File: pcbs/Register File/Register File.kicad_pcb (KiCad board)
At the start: 4 copper layers, 208 parts, among them U201 74HCT574, U202 74HC245, U203 74HC245, U204 74HC245, U301 74HCT574, U302 74HC245, U303 74HC245, U304 74HC245, U401 74HCT574, U402 74HC245, U403 74HC245, U404 74HC245, U501 74HCT574, U502 74HC245, U503 74HC245, U504 74HC245, U601 74HCT574, U602 74HC245, U603 74HC245, U604 74HC245, U701 74HCT574, U702 74HC245, U703 74HC245, U704 74HC245, U801 74HCT574, U802 74HC245, U803 74HC245, U804 74HC245, U901 74HCT574, U902 74HC245, U903 74HC245, U904 74HC245

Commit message: More work
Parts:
- moved U902 87.7 mm to (248.9, 61.0)
- moved R408 71.6 mm to (119.4, 45.7)
- moved R407 71.6 mm to (119.4, 43.2)
- moved R406 71.6 mm to (119.4, 40.6)
- moved R405 71.5 mm to (119.4, 38.1)
- moved R404 71.5 mm to (119.4, 35.6)
- moved R403 71.5 mm to (119.4, 33.0)
- moved R402 71.4 mm to (119.4, 30.5)
- moved R401 71.4 mm to (119.4, 27.9)
- moved D402 71.2 mm to (114.3, 30.5)
- moved D401 71.2 mm to (114.3, 27.9)
- moved D403 71.1 mm to (114.3, 33.0)
- moved D404 71.0 mm to (114.3, 35.6)
- moved D405 71.0 mm to (114.3, 38.1)
- moved D406 70.9 mm to (114.3, 40.6)
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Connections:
- U201 pad 10: unconnected-(U201-GND-Pad10) -> GND
- U201 pad 20: unconnected-(U201-VCC-Pad20) -> +5V
- U202 pad 10: unconnected-(U202-GND-Pad10) -> GND
- U202 pad 20: unconnected-(U202-VCC-Pad20) -> +5V
- U203 pad 10: unconnected-(U203-GND-Pad10) -> GND
- U203 pad 20: unconnected-(U203-VCC-Pad20) -> +5V
- U204 pad 10: unconnected-(U204-GND-Pad10) -> GND
- U204 pad 20: unconnected-(U204-VCC-Pad20) -> +5V
- U301 pad 10: unconnected-(U301-GND-Pad10) -> GND
- U301 pad 20: unconnected-(U301-VCC-Pad20) -> +5V
- U302 pad 10: unconnected-(U302-GND-Pad10) -> GND
- U302 pad 20: unconnected-(U302-VCC-Pad20) -> +5V
- U303 pad 10: unconnected-(U303-GND-Pad10) -> GND
- U303 pad 20: unconnected-(U303-VCC-Pad20) -> +5V
- U304 pad 10: unconnected-(U304-GND-Pad10) -> GND
- U304 pad 20: unconnected-(U304-VCC-Pad20) -> +5V
- U401 pad 10: unconnected-(U401-GND-Pad10) -> GND
- U401 pad 20: unconnected-(U401-VCC-Pad20) -> +5V
- U402 pad 10: unconnected-(U402-GND-Pad10) -> GND
- U402 pad 20: unconnected-(U402-VCC-Pad20) -> +5V
- U403 pad 10: unconnected-(U403-GND-Pad10) -> GND
- U403 pad 20: unconnected-(U403-VCC-Pad20) -> +5V
- U404 pad 10: unconnected-(U404-GND-Pad10) -> GND
- U404 pad 20: unconnected-(U404-VCC-Pad20) -> +5V
- U501 pad 10: unconnected-(U501-GND-Pad10) -> GND
- U501 pad 20: unconnected-(U501-VCC-Pad20) -> +5V
- U502 pad 10: unconnected-(U502-GND-Pad10) -> GND
- U502 pad 20: unconnected-(U502-VCC-Pad20) -> +5V
- U503 pad 10: unconnected-(U503-GND-Pad10) -> GND
- U503 pad 20: unconnected-(U503-VCC-Pad20) -> +5V
- U504 pad 10: unconnected-(U504-GND-Pad10) -> GND
- U504 pad 20: unconnected-(U504-VCC-Pad20) -> +5V
- U601 pad 10: unconnected-(U601-GND-Pad10) -> GND
- U601 pad 2: /Register 4/C0 -> /Register 0/C0
- U601 pad 20: unconnected-(U601-VCC-Pad20) -> +5V
- U601 pad 3: /Register 4/C1 -> /Register 0/C1
- U601 pad 4: /Register 4/C2 -> /Register 0/C2
- U601 pad 5: /Register 4/C3 -> /Register 0/C3
- U601 pad 6: /Register 4/C4 -> /Register 0/C4
- U601 pad 7: /Register 4/C5 -> /Register 0/C5
- U601 pad 8: /Register 4/C6 -> /Register 0/C6
- U601 pad 9: /Register 4/C7 -> /Register 0/C7
- U602 pad 10: unconnected-(U602-GND-Pad10) -> GND
- U602 pad 11: /Register 4/A7 -> /Register 0/A7
- U602 pad 12: /Register 4/A6 -> /Register 0/A6
- U602 pad 13: /Register 4/A5 -> /Register 0/A5
- U602 pad 14: /Register 4/A4 -> /Register 0/A4
- U602 pad 15: /Register 4/A3 -> /Register 0/A3
- U602 pad 16: /Register 4/A2 -> /Register 0/A2
- U602 pad 17: /Register 4/A1 -> /Register 0/A1
- U602 pad 18: /Register 4/A0 -> /Register 0/A0
- U602 pad 20: unconnected-(U602-VCC-Pad20) -> +5V
- U603 pad 10: unconnected-(U603-GND-Pad10) -> GND
- U603 pad 11: /Register 4/B7 -> /Register 0/B7
- U603 pad 12: /Register 4/B6 -> /Register 0/B6
- U603 pad 13: /Register 4/B5 -> /Register 0/B5
- U603 pad 14: /Register 4/B4 -> /Register 0/B4
- U603 pad 15: /Register 4/B3 -> /Register 0/B3
- U603 pad 16: /Register 4/B2 -> /Register 0/B2
- U603 pad 17: /Register 4/B1 -> /Register 0/B1
- U603 pad 18: /Register 4/B0 -> /Register 0/B0
- U603 pad 20: unconnected-(U603-VCC-Pad20) -> +5V
- U604 pad 10: unconnected-(U604-GND-Pad10) -> GND
- U604 pad 11: /Register 4/C7 -> /Register 0/C7
- U604 pad 12: /Register 4/C6 -> /Register 0/C6
- U604 pad 13: /Register 4/C5 -> /Register 0/C5
- U604 pad 14: /Register 4/C4 -> /Register 0/C4
- U604 pad 15: /Register 4/C3 -> /Register 0/C3
- U604 pad 16: /Register 4/C2 -> /Register 0/C2
- U604 pad 17: /Register 4/C1 -> /Register 0/C1
- U604 pad 18: /Register 4/C0 -> /Register 0/C0
- U604 pad 20: unconnected-(U604-VCC-Pad20) -> +5V
- U701 pad 10: unconnected-(U701-GND-Pad10) -> GND
- U701 pad 20: unconnected-(U701-VCC-Pad20) -> +5V
- U702 pad 10: unconnected-(U702-GND-Pad10) -> GND
- U702 pad 20: unconnected-(U702-VCC-Pad20) -> +5V
- U703 pad 10: unconnected-(U703-GND-Pad10) -> GND
- U703 pad 20: unconnected-(U703-VCC-Pad20) -> +5V
- U704 pad 10: unconnected-(U704-GND-Pad10) -> GND
- U704 pad 20: unconnected-(U704-VCC-Pad20) -> +5V
- U801 pad 10: unconnected-(U801-GND-Pad10) -> GND
- U801 pad 20: unconnected-(U801-VCC-Pad20) -> +5V
- U802 pad 10: unconnected-(U802-GND-Pad10) -> GND
- U802 pad 20: unconnected-(U802-VCC-Pad20) -> +5V
- U803 pad 10: unconnected-(U803-GND-Pad10) -> GND
- U803 pad 20: unconnected-(U803-VCC-Pad20) -> +5V
- U804 pad 10: unconnected-(U804-GND-Pad10) -> GND
- U804 pad 20: unconnected-(U804-VCC-Pad20) -> +5V
- U901 pad 10: unconnected-(U901-GND-Pad10) -> GND
- U901 pad 20: unconnected-(U901-VCC-Pad20) -> +5V
- U902 pad 10: unconnected-(U902-GND-Pad10) -> GND
- U902 pad 20: unconnected-(U902-VCC-Pad20) -> +5V
- U903 pad 10: unconnected-(U903-GND-Pad10) -> GND
- U903 pad 20: unconnected-(U903-VCC-Pad20) -> +5V
- U904 pad 10: unconnected-(U904-GND-Pad10) -> GND
- U904 pad 20: unconnected-(U904-VCC-Pad20) -> +5V
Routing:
- net /Register 4/r0: track 0.00 -> 107.5 mm, vias 0 -> 3
- net /Register 5/r0: track 0.00 -> 107.5 mm, vias 0 -> 3
- net /Register 7/r0: track 0.00 -> 107.5 mm, vias 0 -> 3
- net /Register 6/r0: track 0.00 -> 107.5 mm, vias 0 -> 3
- net /Register 5/r1: track 0.00 -> 103.2 mm, vias 0 -> 3
- net /Register 6/r1: track 0.00 -> 103.2 mm, vias 0 -> 3
- net /Register 4/r1: track 0.00 -> 103.2 mm, vias 0 -> 3
- net /Register 7/r1: track 0.00 -> 103.2 mm, vias 0 -> 3
- net /Register 5/r2: track 0.00 -> 98.8 mm, vias 0 -> 3
- net /Register 4/r2: track 0.00 -> 98.8 mm, vias 0 -> 3
- net /Register 7/r2: track 0.00 -> 98.8 mm, vias 0 -> 3
- net /Register 6/r2: track 0.00 -> 98.8 mm, vias 0 -> 3
- net /Register 5/r3: track 0.00 -> 94.5 mm, vias 0 -> 3
- net /Register 4/r3: track 0.00 -> 94.5 mm, vias 0 -> 3
- net /Register 7/r3: track 0.00 -> 94.5 mm, vias 0 -> 3
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
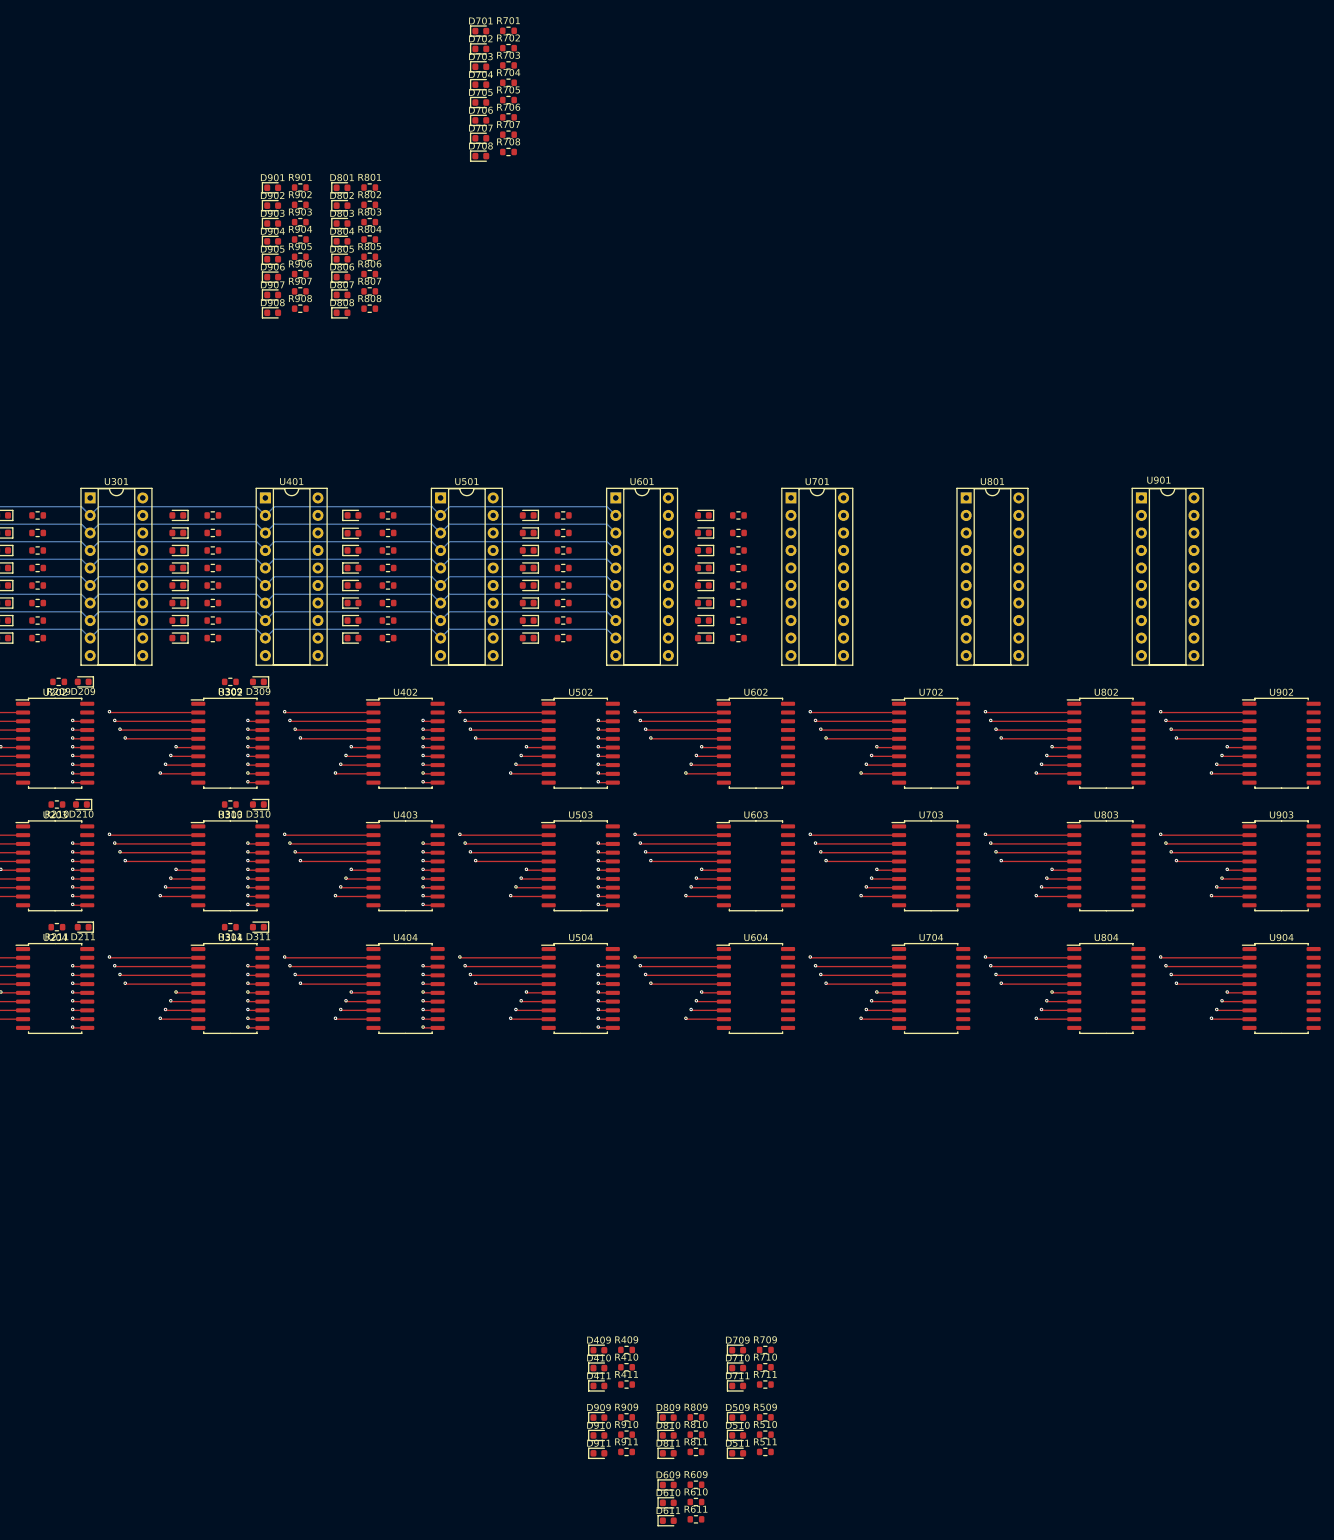
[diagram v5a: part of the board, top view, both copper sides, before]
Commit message: Fixing ordering of registers in schematic
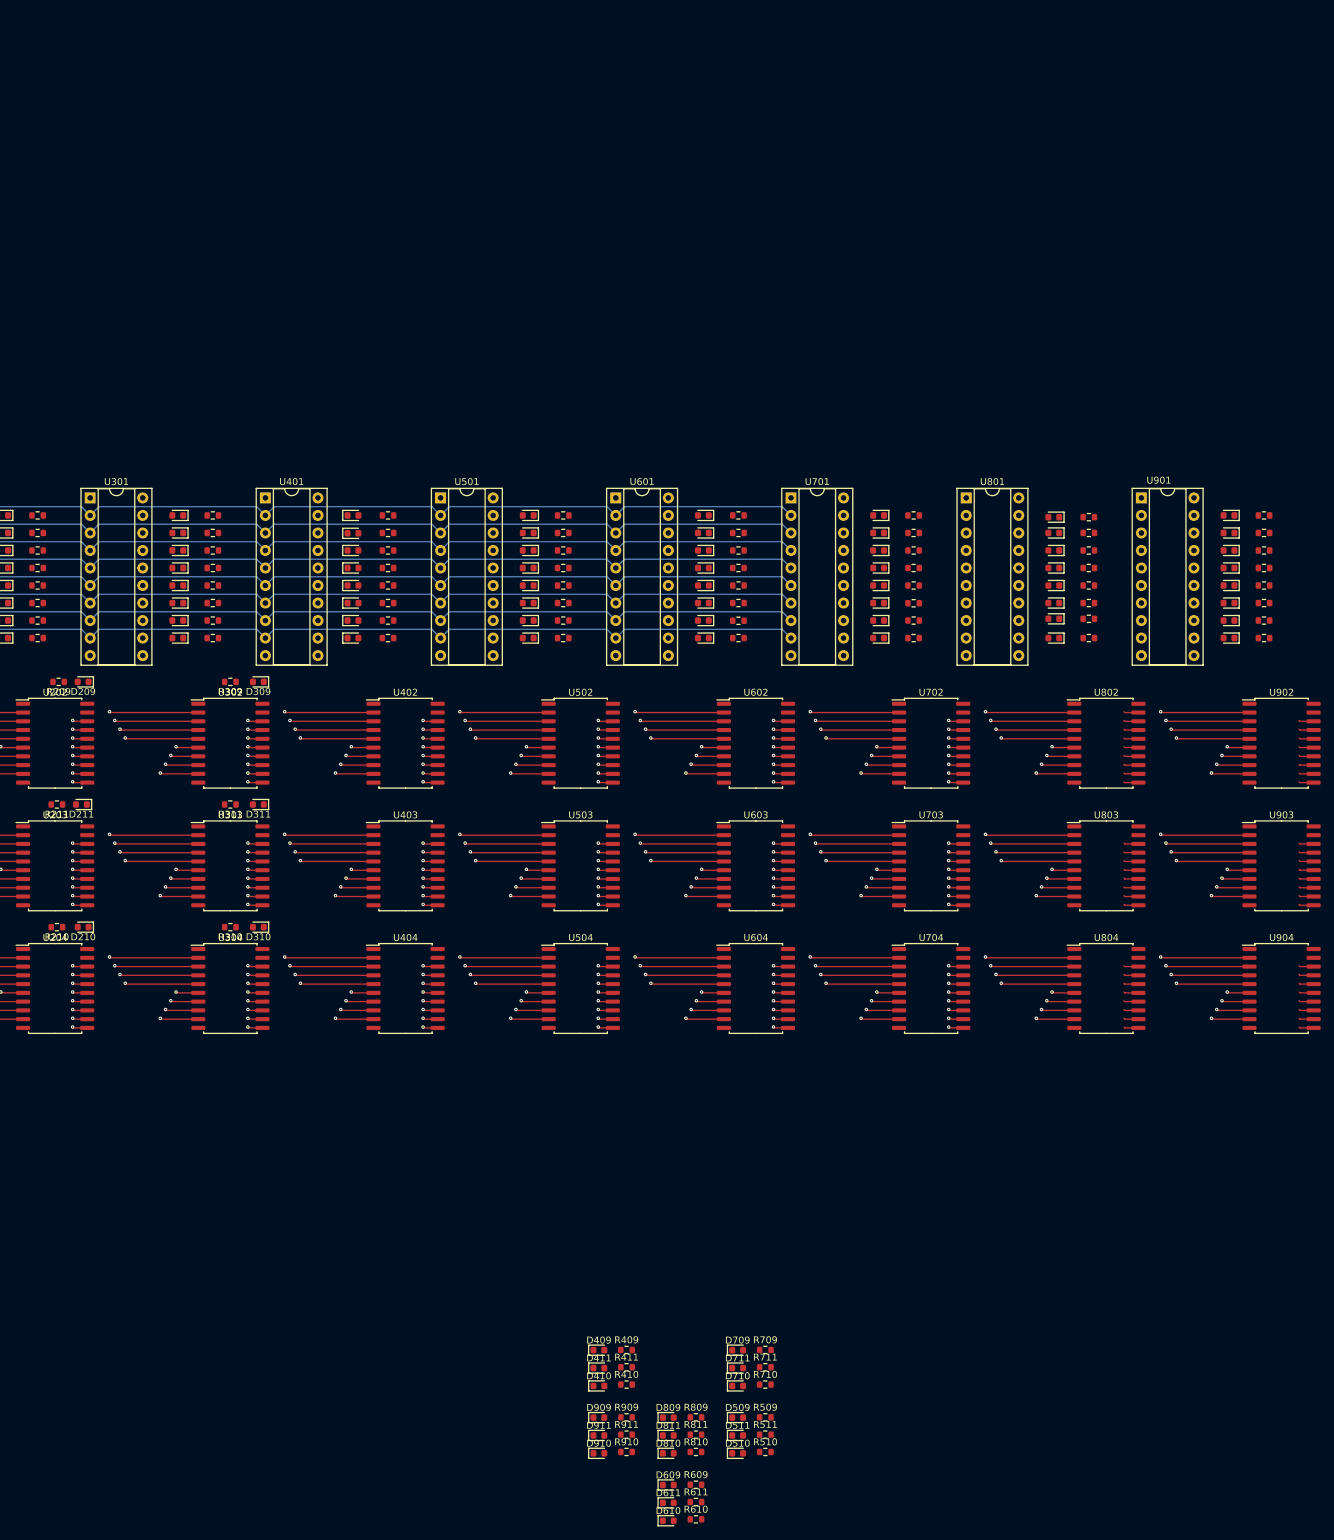
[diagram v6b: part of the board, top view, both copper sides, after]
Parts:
- moved R908 147.7 mm to (246.4, 45.7), turned to 180 degrees
- moved R907 147.6 mm to (246.4, 43.2), turned to 180 degrees
- moved R906 147.6 mm to (246.4, 40.6), turned to 180 degrees
- moved R905 147.6 mm to (246.4, 38.1), turned to 180 degrees
- moved R904 147.6 mm to (246.4, 35.6), turned to 180 degrees
- moved R903 147.6 mm to (246.4, 33.0), turned to 180 degrees
- moved R902 147.6 mm to (246.4, 30.5), turned to 180 degrees
- moved R901 147.6 mm to (246.4, 27.9), turned to 180 degrees
- moved D901 146.6 mm to (241.3, 27.9), turned to 180 degrees
- moved D902 146.5 mm to (241.3, 30.5), turned to 180 degrees
- moved D903 146.5 mm to (241.3, 33.0), turned to 180 degrees
- moved D904 146.5 mm to (241.3, 35.6), turned to 180 degrees
- moved D905 146.5 mm to (241.3, 38.1), turned to 180 degrees
- moved D906 146.5 mm to (241.3, 40.6), turned to 180 degrees
- moved D907 146.5 mm to (241.3, 43.2), turned to 180 degrees
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- renumbered D211 to D210, D210 to D211, D311 to D310, D310 to D311, D411 to D410, D410 to D411, D511 to D510, D510 to D511, D611 to D610, D610 to D611, D711 to D710, D710 to D711, D811 to D810, D810 to D811, D911 to D910, D910 to D911, R211 to R210, R210 to R211, R311 to R310, R310 to R311, R411 to R410, R410 to R411, R511 to R510, R510 to R511, R611 to R610, R610 to R611, R711 to R710, R710 to R711, R811 to R810, R810 to R811, R911 to R910, R910 to R911
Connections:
- D701 pad 2: /Register 7/r0 -> /Register 5/r0
- D702 pad 2: /Register 7/r1 -> /Register 5/r1
- D703 pad 2: /Register 7/r2 -> /Register 5/r2
- D704 pad 2: /Register 7/r3 -> /Register 5/r3
- D705 pad 2: /Register 7/r4 -> /Register 5/r4
- D706 pad 2: /Register 7/r5 -> /Register 5/r5
- D707 pad 2: /Register 7/r6 -> /Register 5/r6
- D708 pad 2: /Register 7/r7 -> /Register 5/r7
- D709 pad 1: /Register 7/~{A_{Enable}} -> /Register 5/~{A_{Enable}}
- D710 pad 1: /Register 7/~{C_{Enable}} -> /Register 5/~{C_{Enable}}
- D711 pad 1: /Register 7/~{B_{Enable}} -> /Register 5/~{B_{Enable}}
- D901 pad 2: /Register 5/r0 -> /Register 7/r0
- D902 pad 2: /Register 5/r1 -> /Register 7/r1
- D903 pad 2: /Register 5/r2 -> /Register 7/r2
- D904 pad 2: /Register 5/r3 -> /Register 7/r3
- D905 pad 2: /Register 5/r4 -> /Register 7/r4
- D906 pad 2: /Register 5/r5 -> /Register 7/r5
- D907 pad 2: /Register 5/r6 -> /Register 7/r6
- D908 pad 2: /Register 5/r7 -> /Register 7/r7
- D909 pad 1: /Register 5/~{A_{Enable}} -> /Register 7/~{A_{Enable}}
- D910 pad 1: /Register 5/~{C_{Enable}} -> /Register 7/~{C_{Enable}}
- D911 pad 1: /Register 5/~{B_{Enable}} -> /Register 7/~{B_{Enable}}
- U701 pad 11: /Register 7/C_{write} -> /Register 5/C_{write}
- U701 pad 12: /Register 7/r7 -> /Register 5/r7
- U701 pad 13: /Register 7/r6 -> /Register 5/r6
- U701 pad 14: /Register 7/r5 -> /Register 5/r5
- U701 pad 15: /Register 7/r4 -> /Register 5/r4
- U701 pad 16: /Register 7/r3 -> /Register 5/r3
- U701 pad 17: /Register 7/r2 -> /Register 5/r2
- U701 pad 18: /Register 7/r1 -> /Register 5/r1
- U701 pad 19: /Register 7/r0 -> /Register 5/r0
- U701 pad 2: /Register 7/C0 -> /Register 0/C0
- U701 pad 3: /Register 7/C1 -> /Register 0/C1
- U701 pad 4: /Register 7/C2 -> /Register 0/C2
- U701 pad 5: /Register 7/C3 -> /Register 0/C3
- U701 pad 6: /Register 7/C4 -> /Register 0/C4
- U701 pad 7: /Register 7/C5 -> /Register 0/C5
- U701 pad 8: /Register 7/C6 -> /Register 0/C6
- U701 pad 9: /Register 7/C7 -> /Register 0/C7
- U702 pad 11: /Register 7/A7 -> /Register 0/A7
- U702 pad 12: /Register 7/A6 -> /Register 0/A6
- U702 pad 13: /Register 7/A5 -> /Register 0/A5
- U702 pad 14: /Register 7/A4 -> /Register 0/A4
- U702 pad 15: /Register 7/A3 -> /Register 0/A3
- U702 pad 16: /Register 7/A2 -> /Register 0/A2
- U702 pad 17: /Register 7/A1 -> /Register 0/A1
- U702 pad 18: /Register 7/A0 -> /Register 0/A0
- U702 pad 19: /Register 7/~{A_{Enable}} -> /Register 5/~{A_{Enable}}
- U702 pad 2: /Register 7/r0 -> /Register 5/r0
- U702 pad 3: /Register 7/r1 -> /Register 5/r1
- U702 pad 4: /Register 7/r2 -> /Register 5/r2
- U702 pad 5: /Register 7/r3 -> /Register 5/r3
- U702 pad 6: /Register 7/r4 -> /Register 5/r4
- U702 pad 7: /Register 7/r5 -> /Register 5/r5
- U702 pad 8: /Register 7/r6 -> /Register 5/r6
- U702 pad 9: /Register 7/r7 -> /Register 5/r7
- U703 pad 11: /Register 7/B7 -> /Register 0/B7
- U703 pad 12: /Register 7/B6 -> /Register 0/B6
- U703 pad 13: /Register 7/B5 -> /Register 0/B5
- U703 pad 14: /Register 7/B4 -> /Register 0/B4
- U703 pad 15: /Register 7/B3 -> /Register 0/B3
- U703 pad 16: /Register 7/B2 -> /Register 0/B2
- U703 pad 17: /Register 7/B1 -> /Register 0/B1
- U703 pad 18: /Register 7/B0 -> /Register 0/B0
- U703 pad 19: /Register 7/~{B_{Enable}} -> /Register 5/~{B_{Enable}}
- U703 pad 2: /Register 7/r0 -> /Register 5/r0
- U703 pad 3: /Register 7/r1 -> /Register 5/r1
- U703 pad 4: /Register 7/r2 -> /Register 5/r2
- U703 pad 5: /Register 7/r3 -> /Register 5/r3
- U703 pad 6: /Register 7/r4 -> /Register 5/r4
- U703 pad 7: /Register 7/r5 -> /Register 5/r5
- U703 pad 8: /Register 7/r6 -> /Register 5/r6
- U703 pad 9: /Register 7/r7 -> /Register 5/r7
- U704 pad 11: /Register 7/C7 -> /Register 0/C7
- U704 pad 12: /Register 7/C6 -> /Register 0/C6
- U704 pad 13: /Register 7/C5 -> /Register 0/C5
- U704 pad 14: /Register 7/C4 -> /Register 0/C4
- U704 pad 15: /Register 7/C3 -> /Register 0/C3
- U704 pad 16: /Register 7/C2 -> /Register 0/C2
- U704 pad 17: /Register 7/C1 -> /Register 0/C1
- U704 pad 18: /Register 7/C0 -> /Register 0/C0
- U704 pad 19: /Register 7/~{C_{Enable}} -> /Register 5/~{C_{Enable}}
- U704 pad 2: /Register 7/r0 -> /Register 5/r0
- U704 pad 3: /Register 7/r1 -> /Register 5/r1
- U704 pad 4: /Register 7/r2 -> /Register 5/r2
- U704 pad 5: /Register 7/r3 -> /Register 5/r3
- U704 pad 6: /Register 7/r4 -> /Register 5/r4
- U704 pad 7: /Register 7/r5 -> /Register 5/r5
- U704 pad 8: /Register 7/r6 -> /Register 5/r6
- U704 pad 9: /Register 7/r7 -> /Register 5/r7
- U901 pad 11: /Register 5/C_{write} -> /Register 7/C_{write}
- U901 pad 12: /Register 5/r7 -> /Register 7/r7
- U901 pad 13: /Register 5/r6 -> /Register 7/r6
- U901 pad 14: /Register 5/r5 -> /Register 7/r5
- U901 pad 15: /Register 5/r4 -> /Register 7/r4
- U901 pad 16: /Register 5/r3 -> /Register 7/r3
- U901 pad 17: /Register 5/r2 -> /Register 7/r2
- U901 pad 18: /Register 5/r1 -> /Register 7/r1
- U901 pad 19: /Register 5/r0 -> /Register 7/r0
- U901 pad 2: /Register 5/C0 -> /Register 7/C0
- U901 pad 3: /Register 5/C1 -> /Register 7/C1
- U901 pad 4: /Register 5/C2 -> /Register 7/C2
- U901 pad 5: /Register 5/C3 -> /Register 7/C3
- U901 pad 6: /Register 5/C4 -> /Register 7/C4
- U901 pad 7: /Register 5/C5 -> /Register 7/C5
- U901 pad 8: /Register 5/C6 -> /Register 7/C6
- U901 pad 9: /Register 5/C7 -> /Register 7/C7
- U902 pad 11: /Register 5/A7 -> /Register 7/A7
- U902 pad 12: /Register 5/A6 -> /Register 7/A6
- U902 pad 13: /Register 5/A5 -> /Register 7/A5
- U902 pad 14: /Register 5/A4 -> /Register 7/A4
- U902 pad 15: /Register 5/A3 -> /Register 7/A3
- U902 pad 16: /Register 5/A2 -> /Register 7/A2
- U902 pad 17: /Register 5/A1 -> /Register 7/A1
- U902 pad 18: /Register 5/A0 -> /Register 7/A0
- U902 pad 19: /Register 5/~{A_{Enable}} -> /Register 7/~{A_{Enable}}
- U902 pad 2: /Register 5/r0 -> /Register 7/r0
- U902 pad 3: /Register 5/r1 -> /Register 7/r1
- U902 pad 4: /Register 5/r2 -> /Register 7/r2
- U902 pad 5: /Register 5/r3 -> /Register 7/r3
- U902 pad 6: /Register 5/r4 -> /Register 7/r4
- U902 pad 7: /Register 5/r5 -> /Register 7/r5
- U902 pad 8: /Register 5/r6 -> /Register 7/r6
- U902 pad 9: /Register 5/r7 -> /Register 7/r7
- U903 pad 11: /Register 5/B7 -> /Register 7/B7
- U903 pad 12: /Register 5/B6 -> /Register 7/B6
- U903 pad 13: /Register 5/B5 -> /Register 7/B5
- U903 pad 14: /Register 5/B4 -> /Register 7/B4
- U903 pad 15: /Register 5/B3 -> /Register 7/B3
- U903 pad 16: /Register 5/B2 -> /Register 7/B2
- U903 pad 17: /Register 5/B1 -> /Register 7/B1
- U903 pad 18: /Register 5/B0 -> /Register 7/B0
- U903 pad 19: /Register 5/~{B_{Enable}} -> /Register 7/~{B_{Enable}}
- U903 pad 2: /Register 5/r0 -> /Register 7/r0
- U903 pad 3: /Register 5/r1 -> /Register 7/r1
- U903 pad 4: /Register 5/r2 -> /Register 7/r2
- U903 pad 5: /Register 5/r3 -> /Register 7/r3
- U903 pad 6: /Register 5/r4 -> /Register 7/r4
- U903 pad 7: /Register 5/r5 -> /Register 7/r5
- U903 pad 8: /Register 5/r6 -> /Register 7/r6
- U903 pad 9: /Register 5/r7 -> /Register 7/r7
- U904 pad 11: /Register 5/C7 -> /Register 7/C7
- U904 pad 12: /Register 5/C6 -> /Register 7/C6
- U904 pad 13: /Register 5/C5 -> /Register 7/C5
- U904 pad 14: /Register 5/C4 -> /Register 7/C4
- U904 pad 15: /Register 5/C3 -> /Register 7/C3
- U904 pad 16: /Register 5/C2 -> /Register 7/C2
- U904 pad 17: /Register 5/C1 -> /Register 7/C1
- U904 pad 18: /Register 5/C0 -> /Register 7/C0
- U904 pad 19: /Register 5/~{C_{Enable}} -> /Register 7/~{C_{Enable}}
- U904 pad 2: /Register 5/r0 -> /Register 7/r0
- U904 pad 3: /Register 5/r1 -> /Register 7/r1
- U904 pad 4: /Register 5/r2 -> /Register 7/r2
- U904 pad 5: /Register 5/r3 -> /Register 7/r3
- U904 pad 6: /Register 5/r4 -> /Register 7/r4
- U904 pad 7: /Register 5/r5 -> /Register 7/r5
- U904 pad 8: /Register 5/r6 -> /Register 7/r6
- U904 pad 9: /Register 5/r7 -> /Register 7/r7
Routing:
- net /Register 0/C6: track 193.4 -> 265.2 mm, vias 4 -> 6
- net /Register 0/C7: track 193.4 -> 265.2 mm, vias 4 -> 6
- net /Register 0/C5: track 193.4 -> 265.0 mm, vias 4 -> 6
- net /Register 0/C4: track 193.4 -> 265.0 mm, vias 4 -> 6
- net /Register 0/C1: track 192.6 -> 264.0 mm, vias 4 -> 6
- net /Register 0/C0: track 192.6 -> 264.0 mm, vias 4 -> 6
- net /Register 0/C3: track 192.6 -> 263.8 mm, vias 4 -> 6
- net /Register 0/C2: track 192.8 -> 264.0 mm, vias 4 -> 6
- net /Register 0/B4: track 87.6 -> 133.0 mm, vias 4 -> 6
- net /Register 0/B5: track 87.6 -> 132.7 mm, vias 4 -> 6
- net /Register 0/A4: track 87.6 -> 132.7 mm, vias 4 -> 6
- net /Register 0/A7: track 87.6 -> 132.7 mm, vias 4 -> 6
- net /Register 0/B6: track 87.6 -> 132.5 mm, vias 4 -> 6
- net /Register 0/B7: track 87.6 -> 132.5 mm, vias 4 -> 6
- net /Register 0/A6: track 87.6 -> 132.5 mm, vias 4 -> 6
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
